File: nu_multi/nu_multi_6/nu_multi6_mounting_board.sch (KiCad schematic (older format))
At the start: 13 parts, among them J1 CONN_01X02, J10 CONN_01X03, J11 CONN_01X02, J12 CONN_01X03, J13 CONN_01X14, J2 CONN_01X03, J3 CONN_01X02, J4 CONN_01X03, J5 CONN_01X02, J6 CONN_01X03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

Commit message: Renamed; use proper names
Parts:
- J1, J11, J3, J5, J7, J9: symbol nu_multi6_output_board:CONN_01X02 -> nu_multi6_mounting_board:CONN_01X02
- J10, J12, J2, J4, J6, J8: symbol nu_multi6_output_board:CONN_01X03 -> nu_multi6_mounting_board:CONN_01X03
- J13: symbol nu_multi6_output_board:CONN_01X14 -> nu_multi6_mounting_board:CONN_01X14
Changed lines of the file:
@@
 $EndDescr
 $Comp
-L nu_multi6_output_board:CONN_01X02 J1
+L nu_multi6_mounting_board:CONN_01X02 J1
 U 1 1 5AA24F79
 P 2050 5220
@@
 $EndComp
 $Comp
-L nu_multi6_output_board:CONN_01X03 J2
+L nu_multi6_mounting_board:CONN_01X03 J2
 U 1 1 5AA2537C
 P 2050 5820
@@
 $EndComp
 $Comp
-L nu_multi6_output_board:CONN_01X02 J3
+L nu_multi6_mounting_board:CONN_01X02 J3
 U 1 1 5AA25639
 P 2050 3770
@@
 $EndComp
 $Comp
-L nu_multi6_output_board:CONN_01X03 J4
+L nu_multi6_mounting_board:CONN_01X03 J4
 U 1 1 5AA2563F
 P 2050 4370
@@
 $EndComp
 $Comp
-L nu_multi6_output_board:CONN_01X02 J5
+L nu_multi6_mounting_board:CONN_01X02 J5
 U 1 1 5AA25CA9
 P 2050 2220
@@
 $EndComp
 $Comp
-L nu_multi6_output_board:CONN_01X03 J6
+L nu_multi6_mounting_board:CONN_01X03 J6
 U 1 1 5AA25CAF
 P 2050 2820
@@
 $EndComp
 $Comp
-L nu_multi6_output_board:CONN_01X02 J7
+L nu_multi6_mounting_board:CONN_01X02 J7
 U 1 1 5AA25CB5
 P 2050 820
@@
 $EndComp
 $Comp
-L nu_multi6_output_board:CONN_01X03 J8
+L nu_multi6_mounting_board:CONN_01X03 J8
 U 1 1 5AA25CBB
 P 2050 1420
@@
 $EndComp
 $Comp
-L nu_multi6_output_board:CONN_01X02 J11
+L nu_multi6_mounting_board:CONN_01X02 J11
 U 1 1 5AA25DFB
 P 2050 6620
@@
 $EndComp
 $Comp
-L nu_multi6_output_board:CONN_01X03 J12
+L nu_multi6_mounting_board:CONN_01X03 J12
 U 1 1 5AA25E01
 P 2050 7220
@@
 $EndComp
 $Comp
-L nu_multi6_output_board:CONN_01X14 J13
+L nu_multi6_mounting_board:CONN_01X14 J13
 U 1 1 5AA25EDC
 P 8800 2770
@@
 CH3
 $Comp
-L nu_multi6_output_board:CONN_01X02 J9
+L nu_multi6_mounting_board:CONN_01X02 J9
 U 1 1 5AA66B7D
 P 5350 920
@@
 $EndComp
 $Comp
-L nu_multi6_output_board:CONN_01X03 J10
+L nu_multi6_mounting_board:CONN_01X03 J10
 U 1 1 5AA66D73
 P 5350 1470

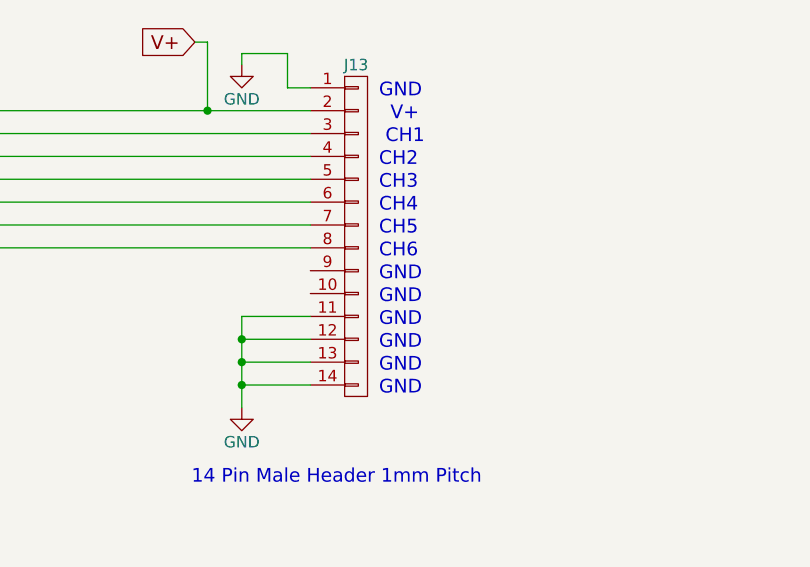
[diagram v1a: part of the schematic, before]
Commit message: Updated label (chan 7 and 8 are NC)
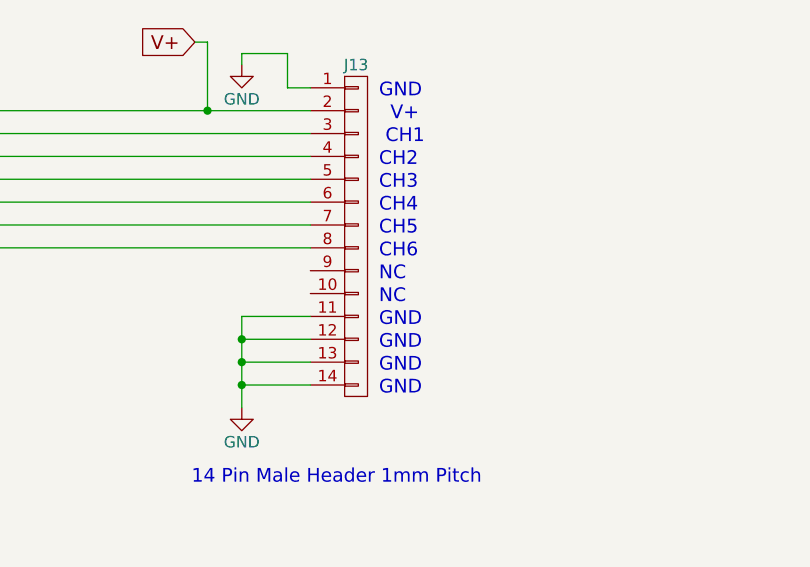
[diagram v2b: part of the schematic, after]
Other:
- note added: "NC"
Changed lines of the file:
@@
 GND
 Text Notes 8900 3070 0    60   ~ 0
-GND
+NC
 Text Notes 8900 2970 0    60   ~ 0
-GND
+NC
 $Comp
 L power:GND #PWR014

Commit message: Moved symbols to global cycfi lib
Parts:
- J1, J11, J3, J5, J7, J9: symbol nu_multi6_mounting_board:CONN_01X02 -> cycfi_library:CONN_01X02
- J10, J12, J2, J4, J6, J8: symbol nu_multi6_mounting_board:CONN_01X03 -> cycfi_library:CONN_01X03
- J13: symbol nu_multi6_mounting_board:CONN_01X14 -> cycfi_library:CONN_01X14
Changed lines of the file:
@@
 $EndDescr
 $Comp
-L nu_multi6_mounting_board:CONN_01X02 J1
+L cycfi_library:CONN_01X02 J1
 U 1 1 5AA24F79
 P 2050 5220
@@
 $EndComp
 $Comp
-L nu_multi6_mounting_board:CONN_01X03 J2
+L cycfi_library:CONN_01X03 J2
 U 1 1 5AA2537C
 P 2050 5820
@@
 $EndComp
 $Comp
-L nu_multi6_mounting_board:CONN_01X02 J3
+L cycfi_library:CONN_01X02 J3
 U 1 1 5AA25639
 P 2050 3770
@@
 $EndComp
 $Comp
-L nu_multi6_mounting_board:CONN_01X03 J4
+L cycfi_library:CONN_01X03 J4
 U 1 1 5AA2563F
 P 2050 4370
@@
 $EndComp
 $Comp
-L nu_multi6_mounting_board:CONN_01X02 J5
+L cycfi_library:CONN_01X02 J5
 U 1 1 5AA25CA9
 P 2050 2220
@@
 $EndComp
 $Comp
-L nu_multi6_mounting_board:CONN_01X03 J6
+L cycfi_library:CONN_01X03 J6
 U 1 1 5AA25CAF
 P 2050 2820
@@
 $EndComp
 $Comp
-L nu_multi6_mounting_board:CONN_01X02 J7
+L cycfi_library:CONN_01X02 J7
 U 1 1 5AA25CB5
 P 2050 820
@@
 $EndComp
 $Comp
-L nu_multi6_mounting_board:CONN_01X03 J8
+L cycfi_library:CONN_01X03 J8
 U 1 1 5AA25CBB
 P 2050 1420
@@
 $EndComp
 $Comp
-L nu_multi6_mounting_board:CONN_01X02 J11
+L cycfi_library:CONN_01X02 J11
 U 1 1 5AA25DFB
 P 2050 6620
@@
 $EndComp
 $Comp
-L nu_multi6_mounting_board:CONN_01X03 J12
+L cycfi_library:CONN_01X03 J12
 U 1 1 5AA25E01
 P 2050 7220
@@
 $EndComp
 $Comp
-L nu_multi6_mounting_board:CONN_01X14 J13
+L cycfi_library:CONN_01X14 J13
 U 1 1 5AA25EDC
 P 8800 2770
@@
 CH3
 $Comp
-L nu_multi6_mounting_board:CONN_01X02 J9
+L cycfi_library:CONN_01X02 J9
 U 1 1 5AA66B7D
 P 5350 920
@@
 $EndComp
 $Comp
-L nu_multi6_mounting_board:CONN_01X03 J10
+L cycfi_library:CONN_01X03 J10
 U 1 1 5AA66D73
 P 5350 1470
